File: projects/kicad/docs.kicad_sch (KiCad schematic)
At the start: 19 parts, among them SW1 SW_PUSH, SW2 SW_PUSH, SW3 SW_PUSH, SW4 SW_PUSH, SW5 SW_PUSH, SW6 SW_PUSH, SW7 RotaryEncoder_Switch, U1 Pico, U3 2.8_240x320_touch_sd_spi

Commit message: Update_0129_yamaguchi
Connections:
- net CS: now also U1.27 (GPIO21); no longer U1.9 (GPIO6)
- net Cal0: now also U1.15 (GPIO11); no longer U1.14 (GPIO10)
- net Cal1: now also U1.12 (GPIO9); no longer U1.15 (GPIO11)
- net DC: now also U1.25 (GPIO19); no longer U1.10 (GPIO7)
- net LED: now also U1.11 (GPIO8); no longer U1.5 (GPIO3)
- net RE_A: now also U1.9 (GPIO6); no longer U1.16 (GPIO12)
- net RE_B: now also U1.10 (GPIO7); no longer U1.17 (GPIO13)
- net RST: now also U1.26 (GPIO20); no longer U1.11 (GPIO8)
- net Row0: now also U1.17 (GPIO13); no longer U1.27 (GPIO21)
- net Row1: now also U1.14 (GPIO10); no longer U1.26 (GPIO20)
- net Row2: now also U1.16 (GPIO12); no longer U1.25 (GPIO19)
- net Row3: now also U1.5 (GPIO3); no longer U1.24 (GPIO18)
- no-connect marks 28 -> 27

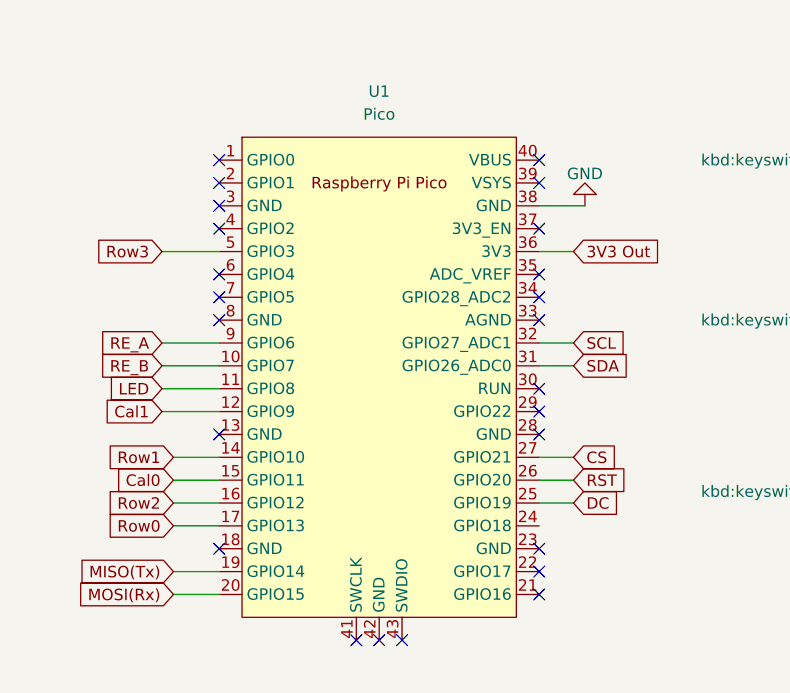
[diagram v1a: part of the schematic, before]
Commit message: yama_update
・LEDの裏表反転
・基盤固定のためのホールを4つ設置
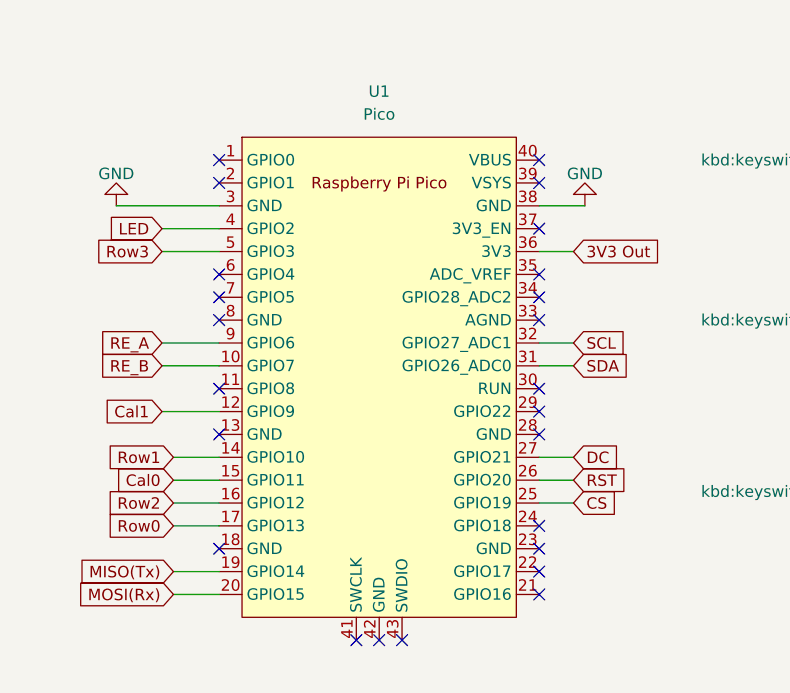
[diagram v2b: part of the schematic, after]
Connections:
- net CS: now also U1.25 (GPIO19); no longer U1.27 (GPIO21)
- net DC: now also U1.27 (GPIO21); no longer U1.25 (GPIO19)
- net GND: now also U1.3 (GND)
- net LED: now also U1.4 (GPIO2); no longer U1.11 (GPIO8)
